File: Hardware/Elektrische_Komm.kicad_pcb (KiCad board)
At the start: 4 copper layers, 127 parts, among them J4 Conn_01x04, J5 USB_OTG, Q1 BSZ014NE2LS5IF, Q10 BSR202NL6327HTSA1, Q11 BSR202NL6327HTSA1, Q12 BSR202NL6327HTSA1, Q13 BSR202NL6327HTSA1, Q14 BSR202NL6327HTSA1, Q2 BSZ014NE2LS5IF, Q3 BSZ014NE2LS5IF, Q4 BSZ014NE2LS5IF, Q5 BSZ014NE2LS5IF, Q6 BSZ014NE2LS5IF, Q7 BSR202NL6327HTSA1, Q8 BSR202NL6327HTSA1, Q9 BSR202NL6327HTSA1, SW1 SW_Push, SW2 SW_Push, U1 TS374IDT, U10 TPS561201, U12 STM32F413R(G-H)Tx_u, U2 UCC27710, U3 ACS723LLCTR, U4 UCC27710, U5 ACS723LLCTR, U6 UCC27710, U7 74HC32D, U8 74LVC2G02, U9 LDK715M50R, Y1 10MHz

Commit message: Layout
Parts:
- added C50: 100n, Capacitors_SMD:C_0603, F.Cu at (193.8, 24.2)
- added C51: 100n, Capacitors_SMD:C_0603, F.Cu at (209.1, 24.8)
- added TP21: TEST, Pin_Headers:Pin_Header_Straight_1x01_Pitch1.00mm, F.Cu at (148.5, 105.0)
- added U11: LVM339IDT, Housings_SOIC:SOIC-14_3.9x8.7mm_Pitch1.27mm, F.Cu at (148.5, 105.0)
- moved R7 150.5 mm to (262.7, 44.2), turned to 180 degrees
- moved U1 146.0 mm to (267.0, 50.2)
- moved R17 143.6 mm to (268.4, 25.9)
- moved R10 142.1 mm to (272.0, 43.5), turned to 90 degrees
- moved C26 142.0 mm to (237.7, 26.2), turned to 270 degrees
- moved R8 134.7 mm to (258.9, 27.7), turned to 90 degrees
- moved C18 128.5 mm to (250.2, 30.5), turned to 180 degrees
- moved C1 124.9 mm to (260.1, 48.9), turned to 180 degrees
- moved D4 123.5 mm to (257.2, 32.0), turned to 180 degrees
- moved D5 121.7 mm to (251.5, 56.9), turned to 90 degrees
- moved R11 121.1 mm to (198.3, 29.1), turned to 270 degrees
- moved U5 118.3 mm to (206.7, 28.9)
- moved R12 118.2 mm to (261.9, 31.0)
- moved C25 114.5 mm to (244.8, 43.1), turned to 90 degrees
- moved R18 114.2 mm to (250.0, 52.6), turned to 90 degrees
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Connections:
- C18 pad 2: Net-(C18-Pad2) -> +3V3
- C20 pad 2: Net-(C20-Pad2) -> +3V3
- C22 pad 2: Net-(C22-Pad2) -> +3V3
- C24 pad 2: Net-(C24-Pad2) -> +3V3
- C26 pad 2: Net-(C26-Pad2) -> +3V3
- D4 pad 4: /D- -> /D+
- D4 pad 6: /D+ -> /D-
- J4 pad 2: (no net) -> /SWDIO
- R12 pad 1: Net-(D4-Pad1) -> Net-(D4-Pad3)
- R14 pad 1: Net-(D4-Pad3) -> Net-(D4-Pad1)
- R8 pad 1: Net-(D4-Pad1) -> Net-(D4-Pad3)
- TP18 pad 1: GNDREF -> /SYSCLK_OUT
- TP20 pad 1: /Sternpunkt_virtuell -> GNDREF
- U12 pad 13: Net-(C26-Pad2) -> +3V3
- U12 pad 19: Net-(C18-Pad2) -> +3V3
- U12 pad 32: Net-(C20-Pad2) -> +3V3
- U12 pad 40: (no net) -> /SYSCLK_OUT
- U12 pad 46: (no net) -> /SWDIO
- U12 pad 48: Net-(C22-Pad2) -> +3V3
- U12 pad 64: Net-(C24-Pad2) -> +3V3
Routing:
- net +3V3: track 0.00 -> 11.3 mm
- net Net-(C3-Pad1): track 0.00 -> 11.1 mm
- net /SWDIO: track 0.00 -> 10.9 mm
- net Net-(C7-Pad1): track 0.00 -> 10.5 mm
- net /SWCLK: track 0.00 -> 6.24 mm
- net /A_conn: track 0.00 -> 5.83 mm
- net +5V: track 0.00 -> 5.21 mm
- net Net-(C2-Pad1): track 0.00 -> 4.16 mm
- net Net-(J5-Pad3): track 0.00 -> 4.07 mm
- net Net-(J5-Pad2): track 0.00 -> 4.02 mm
- net /Curr_direct_B: track 0.00 -> 3.88 mm
- net /Curr_direct_A: track 0.00 -> 3.75 mm
- net /Vin: track 0.00 -> 3.43 mm
- net Net-(D4-Pad3): track 0.00 -> 2.86 mm
- net Net-(D4-Pad1): track 0.00 -> 2.84 mm
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- added copper zone on F.Cu, net /A_conn
- added copper zone on F.Cu, net Net-(C2-Pad1)
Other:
- net class Diff_pair removed
- rule pad_to_mask_clearance: 0.2 -> 0

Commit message: Layout
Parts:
- moved Y1 109.6 mm to (230.8, 32.5), turned to 90 degrees
- moved C21 107.9 mm to (226.8, 30.7)
- moved C23 105.5 mm to (226.8, 34.3)
- moved C19 67.1 mm to (136.5, 39.0)
- moved R40 67.0 mm to (141.5, 38.4), turned to 270 degrees
- moved Q7 65.6 mm to (131.6, 41.7), turned to 180 degrees
- moved R32 63.3 mm to (140.0, 42.3), turned to 90 degrees
- moved U11 60.7 mm to (145.3, 44.4), turned to 90 degrees
- moved R27 59.5 mm to (132.0, 47.9)
- moved R28 56.5 mm to (140.0, 49.1), turned to 90 degrees
- moved R22 55.6 mm to (141.7, 49.8), turned to 90 degrees
- moved C11 55.4 mm to (138.6, 50.5), turned to 270 degrees
- moved C17 55.0 mm to (144.0, 50.2), turned to 270 degrees
- moved U7 11.6 mm to (136.5, 44.9), turned to 270 degrees
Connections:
- U7 pad 11: /OR2 -> /OR1
- U7 pad 12: Net-(R32-Pad2) -> Net-(R22-Pad2)
- U7 pad 13: Net-(R40-Pad2) -> Net-(R28-Pad2)
- U7 pad 4: Net-(R22-Pad2) -> Net-(R32-Pad2)
- U7 pad 5: Net-(R28-Pad2) -> Net-(R40-Pad2)
- U7 pad 6: /OR1 -> /OR2
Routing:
- net Net-(Q7-Pad3): track 0.00 -> 15.5 mm
- net /Stop: track 0.00 -> 13.1 mm
- net Net-(R22-Pad2): track 0.00 -> 11.6 mm
- net Net-(R40-Pad2): track 0.00 -> 11.1 mm, vias 0 -> 2
- net Net-(C21-Pad2): track 0.00 -> 8.79 mm
- net Net-(R32-Pad2): track 0.00 -> 8.74 mm, vias 0 -> 2
- net Net-(C23-Pad2): track 0.00 -> 8.56 mm
- net Net-(R28-Pad2): track 0.00 -> 7.11 mm
- net /OR2: track 0.00 -> 6.98 mm, vias 0 -> 2
- net /OR1: track 0.00 -> 6.71 mm
- net /freigegeben: track 0.00 -> 5.82 mm
- net /Over_curr: track 0.00 -> 4.06 mm
- net +3V3: track 11.3 -> 14.3 mm
- net +5V: track 5.21 -> 7.50 mm
- net Net-(R27-Pad2): track 0.00 -> 1.86 mm
- added copper zone on F.Cu, net Net-(C21-Pad2)
- added copper zone on F.Cu, net Net-(C23-Pad2)

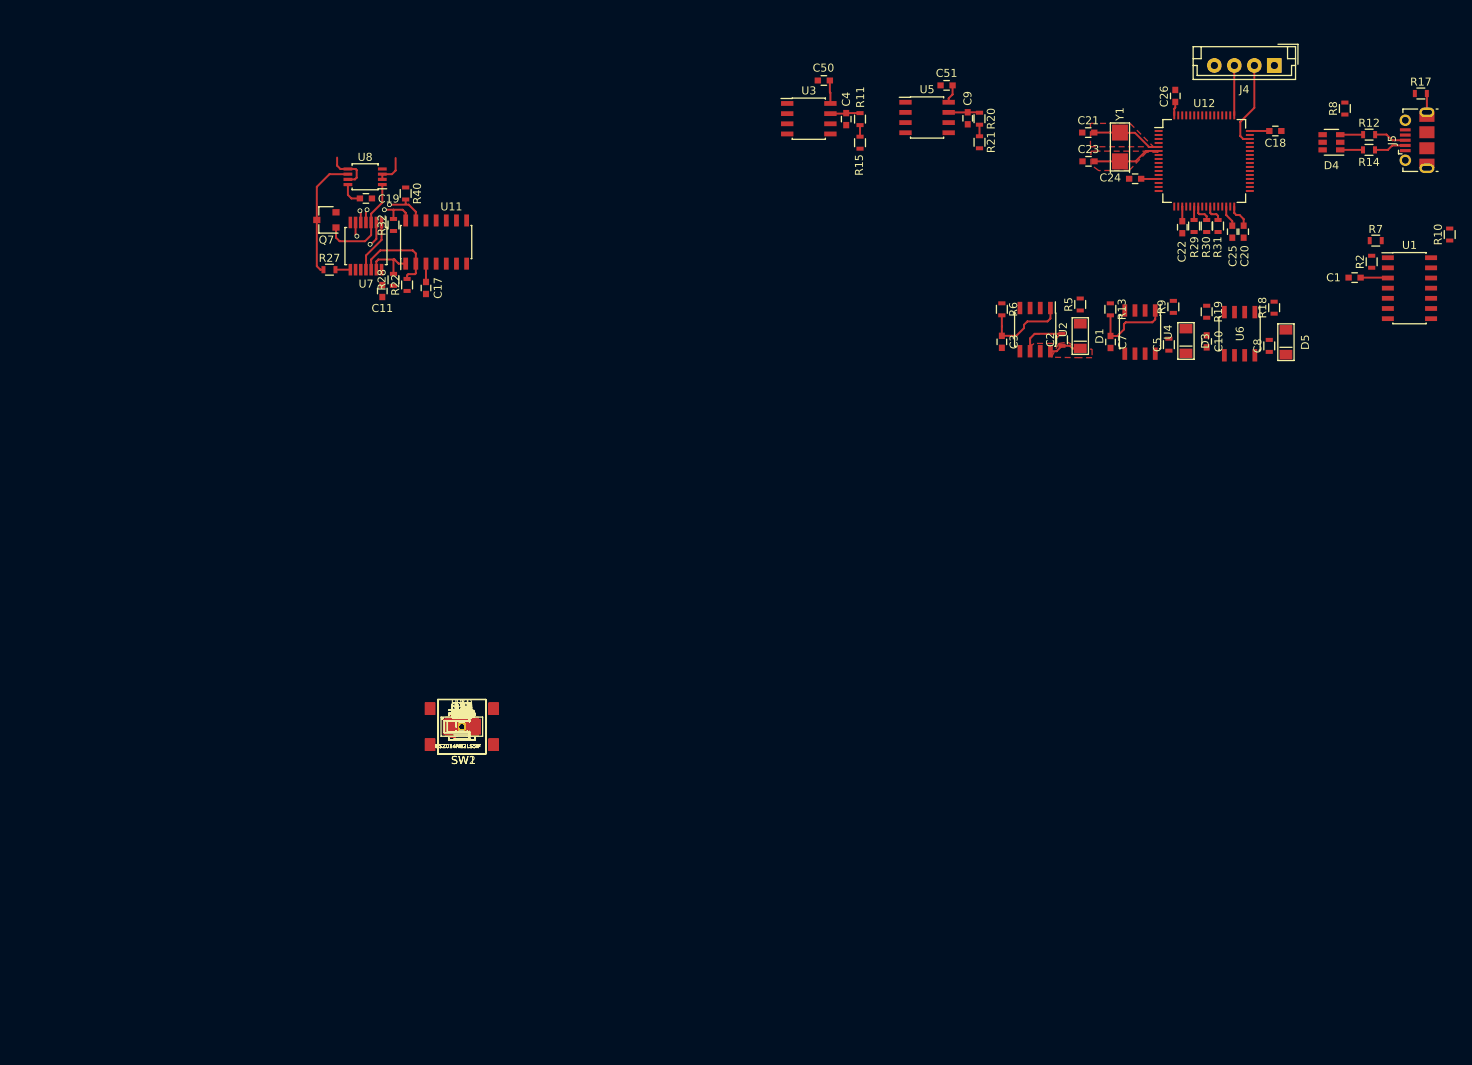
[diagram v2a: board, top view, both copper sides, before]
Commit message: Korrektur Strommessung
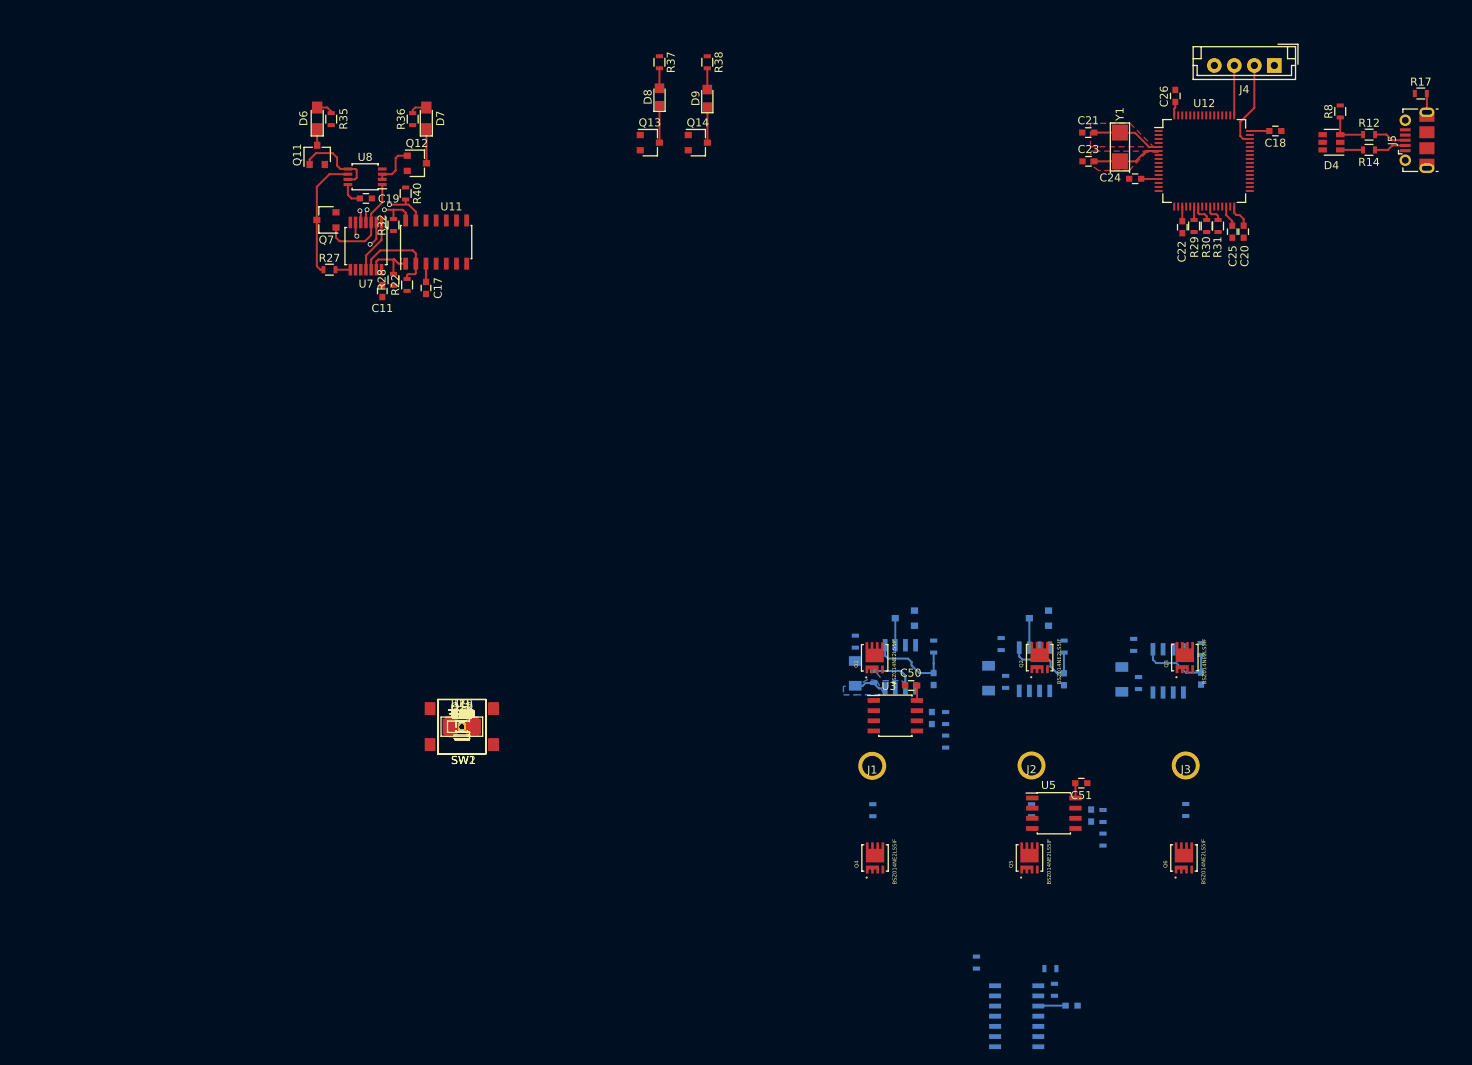
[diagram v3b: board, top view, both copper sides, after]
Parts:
- added J1: Conn_01x01, kicadBibs:MotorConn, F.Cu at (199.8, 109.9)
- added J2: Conn_01x01, kicadBibs:MotorConn, F.Cu at (219.7, 109.9)
- added J3: Conn_01x01, kicadBibs:MotorConn, F.Cu at (239.0, 109.9)
- C1, C10, C2, C3, C4, C5, C7, C8, C9, D1, D3, D5, Q8, Q9, R1, R10, R11, R13, R15, R18, R19, R2, R20, R21, R3, R4, R5, R6, R7, R9, U1, U2, U4, U6: moved to B.Cu
- moved R10 108.5 mm to (212.8, 134.5)
- moved U1 103.4 mm to (217.9, 141.2), turned to 180 degrees
- moved R7 99.7 mm to (222.1, 135.3), turned to 0 degrees
- moved R2 99.3 mm to (222.6, 137.9)
- moved C1 97.6 mm to (224.7, 139.9), turned to 0 degrees
- moved Q6 91.7 mm to (238.8, 121.4), turned to 90 degrees
- moved R4 91.1 mm to (239.0, 115.4), turned to 90 degrees
- moved Q3 90.8 mm to (238.9, 96.4), turned to 90 degrees
- moved C51 88.8 mm to (225.9, 112.1), turned to 0 degrees
- moved R38 88.5 mm to (179.2, 21.9), turned to 270 degrees
- moved C9 88.5 mm to (227.2, 116.1)
- moved R20 88.5 mm to (228.6, 116.2)
- moved R21 88.5 mm to (228.6, 119.1)
- moved U5 88.4 mm to (222.5, 115.8)
- moved R37 86.6 mm to (173.2, 21.9), turned to 270 degrees
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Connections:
- Q2 pad 2: /B -> /B_conn
- Q4 pad 3: /A -> /A_conn
- U5 pad 1: /B -> /B_conn
- U5 pad 2: /B -> /B_conn
- U5 pad 3: /B_conn -> /B
- U5 pad 4: /B_conn -> /B
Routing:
- net Net-(C10-Pad1): track 0.00 -> 10.2 mm
- net /freigegeben: track 5.82 -> 10.4 mm
- net Net-(D8-Pad1): track 0.00 -> 4.61 mm
- net Net-(D9-Pad1): track 0.00 -> 4.45 mm
- net Net-(D7-Pad1): track 0.00 -> 4.28 mm
- net /Curr_direct_B: track 3.88 -> 0.00 mm
- net /Curr_direct_A: track 3.75 -> 0.00 mm
- net /HI_B_F: track 0.00 -> 3.69 mm
- net /HI_A_F: track 0.00 -> 3.38 mm
- net Net-(D9-Pad2): track 0.00 -> 2.66 mm
- net Net-(D8-Pad2): track 0.00 -> 2.49 mm
- net Net-(D7-Pad2): track 0.00 -> 2.21 mm
- net Net-(D6-Pad2): track 0.00 -> 2.16 mm
- net Net-(D4-Pad3): track 2.86 -> 5.01 mm
- net Net-(D6-Pad1): track 0.00 -> 2.02 mm
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- added copper zone on B.Cu, net /A_conn
- added copper zone on B.Cu, net Net-(C2-Pad1)
- removed copper zone on F.Cu, net /A_conn
- removed copper zone on F.Cu, net Net-(C2-Pad1)

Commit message: Zwei Strommesser
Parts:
- Q10: moved to B.Cu
- moved TP18 125.1 mm to (251.8, 34.5)
- moved R41 107.2 mm to (232.7, 38.6), turned to 180 degrees
- moved SW1 99.7 mm to (226.3, 42.6), turned to 90 degrees
- moved Q10 89.9 mm to (237.3, 91.4), turned to 180 degrees
- moved Q13 61.9 mm to (233.6, 25.5), turned to 90 degrees
- moved Q14 56.5 mm to (233.5, 21.2), turned to 90 degrees
- moved D8 56.0 mm to (229.2, 26.5), turned to 180 degrees
- moved R37 55.8 mm to (229.0, 24.6), turned to 180 degrees
- moved D9 50.2 mm to (229.2, 22.3), turned to 180 degrees
- moved R38 49.7 mm to (228.9, 20.3), turned to 180 degrees
- moved C1 17.0 mm to (213.7, 127.0), turned to 180 degrees
- moved U1 15.8 mm to (220.6, 125.7), turned to 0 degrees
- moved R2 11.2 mm to (215.8, 129.0), turned to 270 degrees
- moved R10 10.2 mm to (222.5, 131.3), turned to 180 degrees
- moved R7 6.32 mm to (217.1, 131.3), turned to 180 degrees
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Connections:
- U12 pad 55: /Hochlauf -> /elekKomm
- U12 pad 56: /elekKomm -> /Hochlauf
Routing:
- net /Sternpunkt_virtuell: track 0.00 -> 61.1 mm
- net /A_conn: track 5.83 -> 38.9 mm
- net /C: track 0.00 -> 29.3 mm
- net /B_conn: track 0.00 -> 16.6 mm, vias 0 -> 2
- net /elekKomm: track 0.00 -> 14.3 mm
- net /Hochlauf: track 0.00 -> 12.8 mm
- net /NRST: track 0.00 -> 10.8 mm
- net /SYSCLK_OUT: track 0.00 -> 4.84 mm
- net /HI_C_F: track 0.00 -> 3.90 mm
- net /Bemf_A: track 0.00 -> 2.03 mm
- net /Bemf_C: track 0.00 -> 1.87 mm
- net /Bemf_B: track 0.00 -> 1.86 mm
- net Net-(D9-Pad2): track 2.66 -> 2.00 mm
- net Net-(D8-Pad2): track 2.49 -> 1.95 mm
- added copper zone on B.Cu, net /Sternpunkt_virtuell

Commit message: _______________ < Neue Bauteile >  ---------------       \                    / \  //\        \    |\___/|      /   \//  \\             /0  0  \__  /    //  | \ \            /     /  \/_/    //   |  \  \            @_^_@'/   \/_   //    |   \   \            //_^_/     \/_ //     |    \    \         ( //) |        \///      |     \     \       ( / /) _|_ /   )  //       |      \     _\     ( // /) '/,_ _ _/  ( ; -.    |    _ _\.-~        .-~~~^-.   (( / / )) ,-{        _      `-.|.-~-.           .~         `.  (( // / ))  '/\      /                 ~-. _ .-~      .-~^-.  \  (( /// ))      `.   {            }                   /      \  \   (( / ))     .----~-.\        \-'                 .~         \  `. \^-.              ///.----..>        \             _ -~             `.  ^-`  ^-_                ///-._ _ _ _ _ _ _}^ - - - - ~                     ~-- ,.-~                                                                   /.-~
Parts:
- removed C14, C51: 100n, Capacitors_SMD:C_0603
- removed C15: 470n, Capacitors_SMD:C_0603
- removed C9: 10n, Capacitors_SMD:C_0603
- removed R11, R15, R20, R21, R33, R34: R, Resistors_SMD:R_0603
- removed R12, R14: 27, Resistors_SMD:R_0603
- removed R32, R40: 10k, Resistors_SMD:R_0603
- removed R8: 1,5k, Resistors_SMD:R_0603
- removed U5: ACS723LLCTR, Housings_SOIC:SOIC-8_3.9x4.9mm_Pitch1.27mm
- removed U9: LDK715M50R, TO_SOT_Packages_SMD:SOT-23-5_HandSoldering
- added R50: R, Resistors_SMD:R_0603, F.Cu at (205.9, 43.4)
- added R51: R, Resistors_SMD:R_0603, F.Cu at (203.1, 43.4)
- added TP22, TP23, TP24, TP25: TEST, Pin_Headers:Pin_Header_Straight_1x01_Pitch1.00mm, F.Cu at (179.3, 45.2)
- C4: moved to F.Cu
- U11: value LVM339IDT -> TLC352; footprint Housings_SOIC:SOIC-14_3.9x8.7mm_Pitch1.27mm -> Housings_SSOP:TSSOP-8_4.4x3mm_Pitch0.65mm
- Y1: value 10MHz -> 24MHz
- moved R23 95.2 mm to (206.8, 29.7), turned to 180 degrees
- moved R42 94.6 mm to (198.5, 24.8), turned to 270 degrees
- moved R25 93.4 mm to (203.8, 29.7), turned to 180 degrees
- moved D6 91.3 mm to (221.2, 19.7), turned to 0 degrees
- moved SW2 89.6 mm to (191.2, 26.2)
- moved R35 89.3 mm to (221.1, 21.5), turned to 0 degrees
- moved Q11 87.3 mm to (216.7, 19.7), turned to 0 degrees
- moved Q7 79.7 mm to (208.5, 20.9), turned to 90 degrees
- moved U8 78.2 mm to (213.9, 25.7), turned to 90 degrees
- moved C19 75.9 mm to (211.2, 25.8), turned to 270 degrees
- moved R36 75.8 mm to (218.1, 31.1), turned to 0 degrees
- moved R27 75.2 mm to (202.3, 21.2), turned to 270 degrees
- moved R39 74.7 mm to (203.1, 54.0), turned to 270 degrees
- moved D7 74.3 mm to (218.2, 32.8), turned to 0 degrees
- moved D10 72.3 mm to (203.1, 57.6), turned to 90 degrees
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- renumbered D9 to D8, D8 to D9
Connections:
- C1 pad 1: /Vin -> (no net)
- C16 pad 1: +15V -> /DCDC_EN
- C17 pad 1: +5V -> +3V3
- C50 pad 1: +5V -> +3V3
- D4 pad 1: Net-(D4-Pad1) -> /D+
- D4 pad 3: Net-(D4-Pad3) -> /D-
- D4 pad 4: /D+ -> Net-(D4-Pad4)
- D4 pad 5: (no net) -> Net-(D4-Pad5)
- D4 pad 6: /D- -> Net-(D4-Pad6)
- D8 pad 1: Net-(D9-Pad1) -> Net-(D8-Pad1)
- D8 pad 2: Net-(D9-Pad2) -> Net-(D8-Pad2)
- D9 pad 1: Net-(D8-Pad1) -> Net-(D9-Pad1)
- D9 pad 2: Net-(D8-Pad2) -> Net-(D9-Pad2)
- J1 pad 1: /A_conn -> /A
- J2 pad 1: /B_conn -> /B
- J5 pad 1: (no net) -> Net-(D4-Pad5)
- J5 pad 2: Net-(J5-Pad2) -> Net-(D4-Pad4)
- J5 pad 3: Net-(J5-Pad3) -> Net-(D4-Pad6)
- Q1 pad 3: +15V -> /Meas_out
- Q2 pad 2: /B_conn -> /B
- Q2 pad 3: +15V -> /Meas_out
- Q3 pad 3: +15V -> /Meas_out
- Q4 pad 3: /A_conn -> /A
- R1 pad 2: /A_conn -> /A
- R13 pad 1: +15V -> /DCDC_EN
- R16 pad 1: +15V -> /DCDC_EN
- R19 pad 1: +15V -> /DCDC_EN
- R23 pad 1: +5V -> +3V3
- R3 pad 2: /B_conn -> /B
- R6 pad 1: +15V -> /DCDC_EN
- TP12 pad 1: +5V -> /LI_B
- TP16 pad 1: +15V -> /DCDC_EN
- TP4 pad 1: /Curr_direct_B -> /LI_A
- U1 pad 3: /Vin -> /DCDC_EN
- U10 pad 3: +15V -> /DCDC_EN
- U10 pad 5: +15V -> /DCDC_EN
- U11 pad 1: Net-(R28-Pad2) -> Net-(R22-Pad2)
- U11 pad 2: Net-(R22-Pad2) -> /Curr_direct_A
- U11 pad 3: +5V -> Net-(R23-Pad2)
- U11 pad 4: Net-(R23-Pad2) -> GNDREF
- U11 pad 6: Net-(R23-Pad2) -> Net-(R50-Pad2)
- U11 pad 7: /Curr_direct_B -> Net-(R28-Pad2)
- U11 pad 8: /Curr_direct_B -> +3V3
- U12 pad 14: /LI_A -> /LI_C
- U12 pad 16: /LI_C -> /LI_A
- U12 pad 24: /Curr_mcu_A -> /Curr_direct_A
- U12 pad 25: /Curr_mcu_B -> (no net)
- U12 pad 55: /elekKomm -> (no net)
- U12 pad 56: /Hochlauf -> /freigegeben
- U12 pad 58: (no net) -> /StopMCU
- U12 pad 59: (no net) -> /Over_curr
- U12 pad 61: (no net) -> /elekKomm
- U12 pad 62: (no net) -> /Hochlauf
- U12 pad 8: /A_conn -> /A
- U12 pad 9: /B_conn -> /B
- U3 pad 1: /A -> /DCDC_EN
- U3 pad 2: /A -> /DCDC_EN
- U3 pad 3: /A_conn -> /Meas_out
- U3 pad 4: /A_conn -> /Meas_out
- U3 pad 8: +5V -> +3V3
- U7 pad 2: /OR2 -> /StopMCU
- U7 pad 4: Net-(R32-Pad2) -> (no net)
- U7 pad 5: Net-(R40-Pad2) -> (no net)
- U7 pad 6: /OR2 -> (no net)
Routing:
- net /StopMCU: track 0.00 -> 42.9 mm, vias 0 -> 6
- net /Freigabe_MCU: track 0.00 -> 41.7 mm, vias 0 -> 2
- net /A_conn: track 38.9 -> 5.83 mm
- net /freigegeben: track 10.4 -> 41.1 mm, vias 0 -> 2
- net /Over_curr: track 5.64 -> 32.4 mm
- net /Curr_direct_A: track 0.00 -> 22.8 mm, vias 0 -> 2
- net /B_conn: track 16.6 -> 0.00 mm, vias 2 -> 0
- net /Freigabe_button: track 0.00 -> 15.3 mm
- net Net-(R40-Pad2): track 11.1 -> 0.00 mm, vias 2 -> 0
- net Net-(R28-Pad2): track 7.11 -> 17.8 mm
- net /Sternpunkt_virtuell: track 61.1 -> 50.5 mm
- net /A: track 0.00 -> 10.0 mm
- net Net-(R32-Pad2): track 8.74 -> 0.00 mm, vias 2 -> 0
- net /NRST: track 10.8 -> 18.8 mm
- net /OR2: track 6.98 -> 0.00 mm, vias 2 -> 0
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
